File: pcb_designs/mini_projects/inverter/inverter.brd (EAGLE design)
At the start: 48.2 x 46.7 mm, 8 parts, among them IC1 4047, Q1 IRFZ44, Q2 IRFZ44

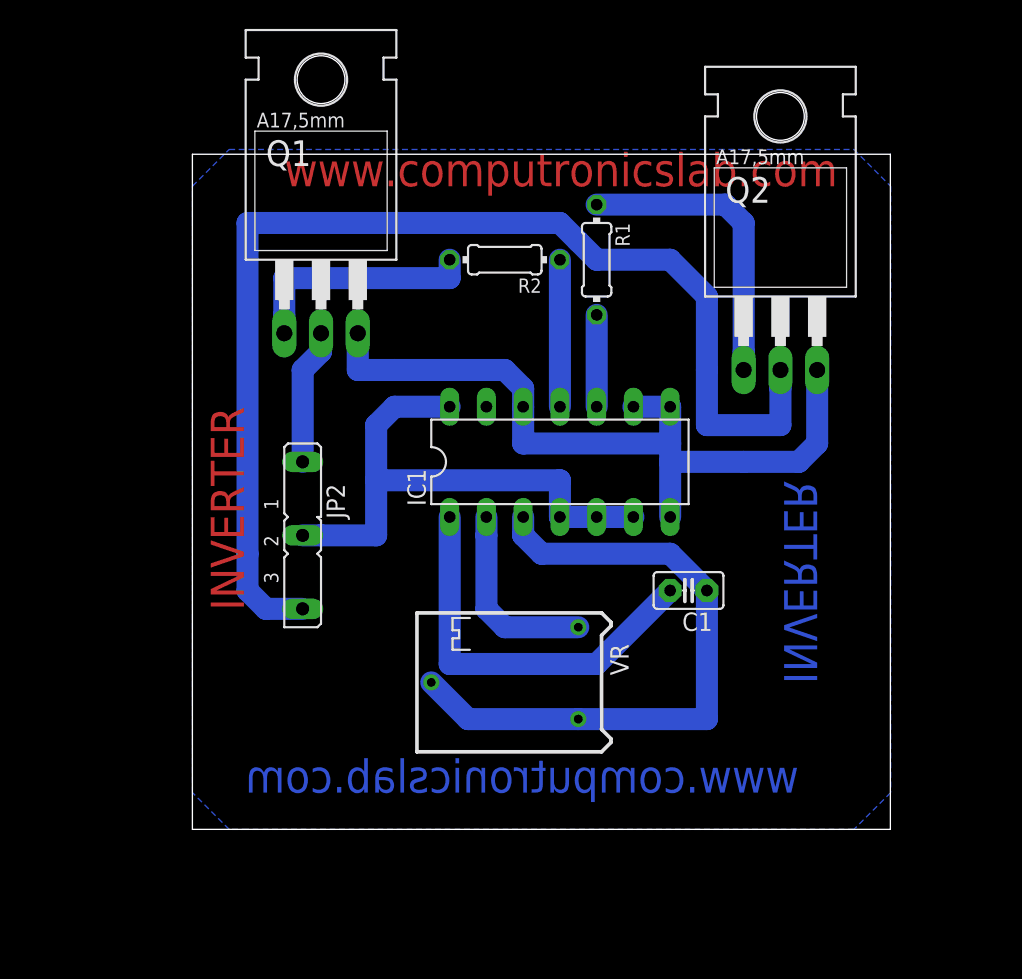
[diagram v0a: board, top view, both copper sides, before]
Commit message: 
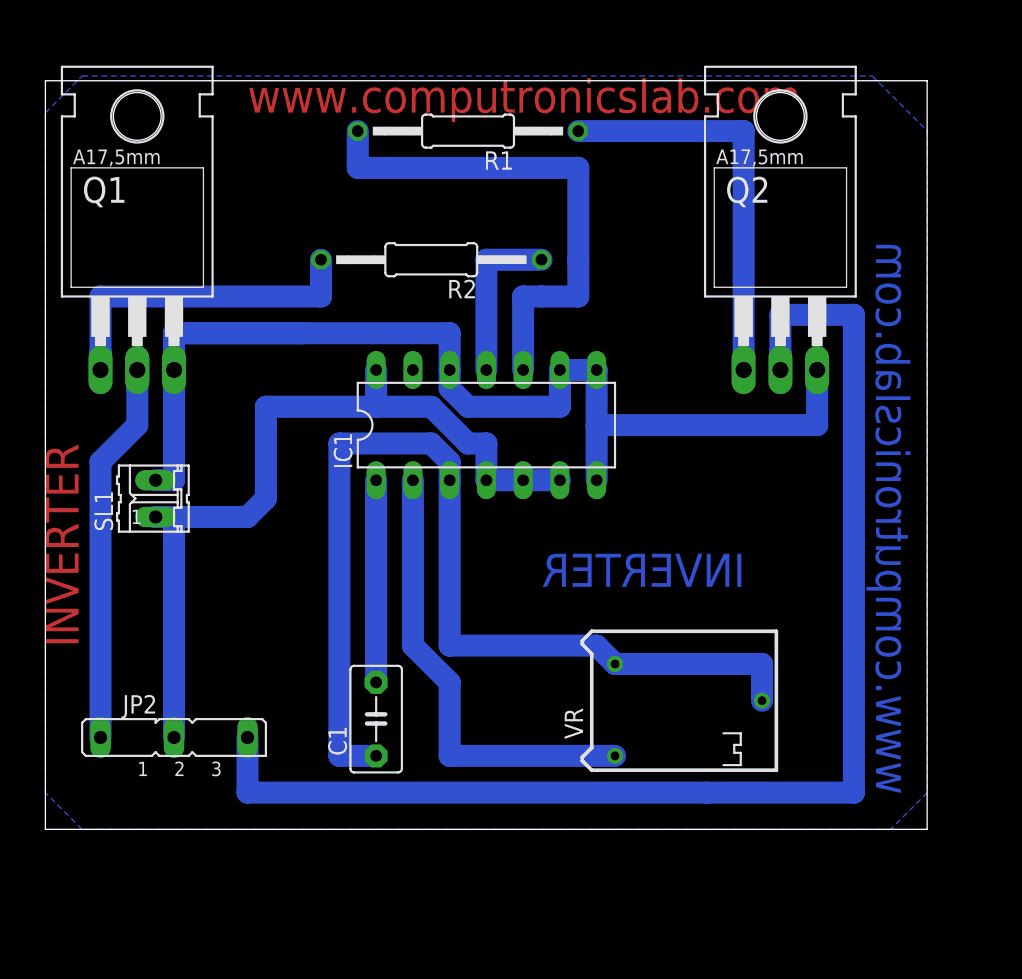
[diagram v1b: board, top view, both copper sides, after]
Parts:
- added SL1: battery, con-amp-quick:02P
- C1: device capacitor-wima:C2.5-2 -> capacitor-wima:C5B3.5
- R1, R2: device rcl:0204/7 -> rcl:0207/15
- moved C1 23.3 mm to (34.3, 34.3), turned to 90 degrees
- moved JP2 16.6 mm to (20.3, 33.0), turned to 0 degrees
- moved Q1 13.0 mm to (17.8, 64.8)
- moved R1 12.6 mm to (40.6, 74.9), turned to 180 degrees
- moved VR 7.73 mm to (53.3, 35.6), turned to 0 degrees
- moved IC1 5.68 mm to (41.9, 54.6)
- moved R2 5.08 mm to (38.1, 66.0)
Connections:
- net N$5: now also SL1.2
- net N$8: now also SL1.1
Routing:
- net N$5: track 54.4 -> 85.6 mm
- net N$3: track 6.35 -> 35.6 mm
- net N$12: track 44.5 -> 69.6 mm
- net N$8: track 38.6 -> 57.5 mm
- net N$11: track 13.2 -> 31.5 mm
- net N$6: track 9.42 -> 26.5 mm
- net N$10: track 27.5 -> 14.0 mm
- net N$2: track 20.8 -> 27.9 mm
- net N$4: track 16.5 -> 22.9 mm
- net N$7: track 81.4 -> 87.6 mm
- net N$1: track 10.2 -> 11.4 mm
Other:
- board size 48.2 x 46.7 mm -> 60.9 x 51.7 mm
